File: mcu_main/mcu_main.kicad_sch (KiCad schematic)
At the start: 23 parts, among them SW1 SW_Push_Dual, SW2 SW_Push_Dual, U1 ESP32-S3-WROOM-1, U3 SGM2212-3.3, U5 SGM2212-2.8

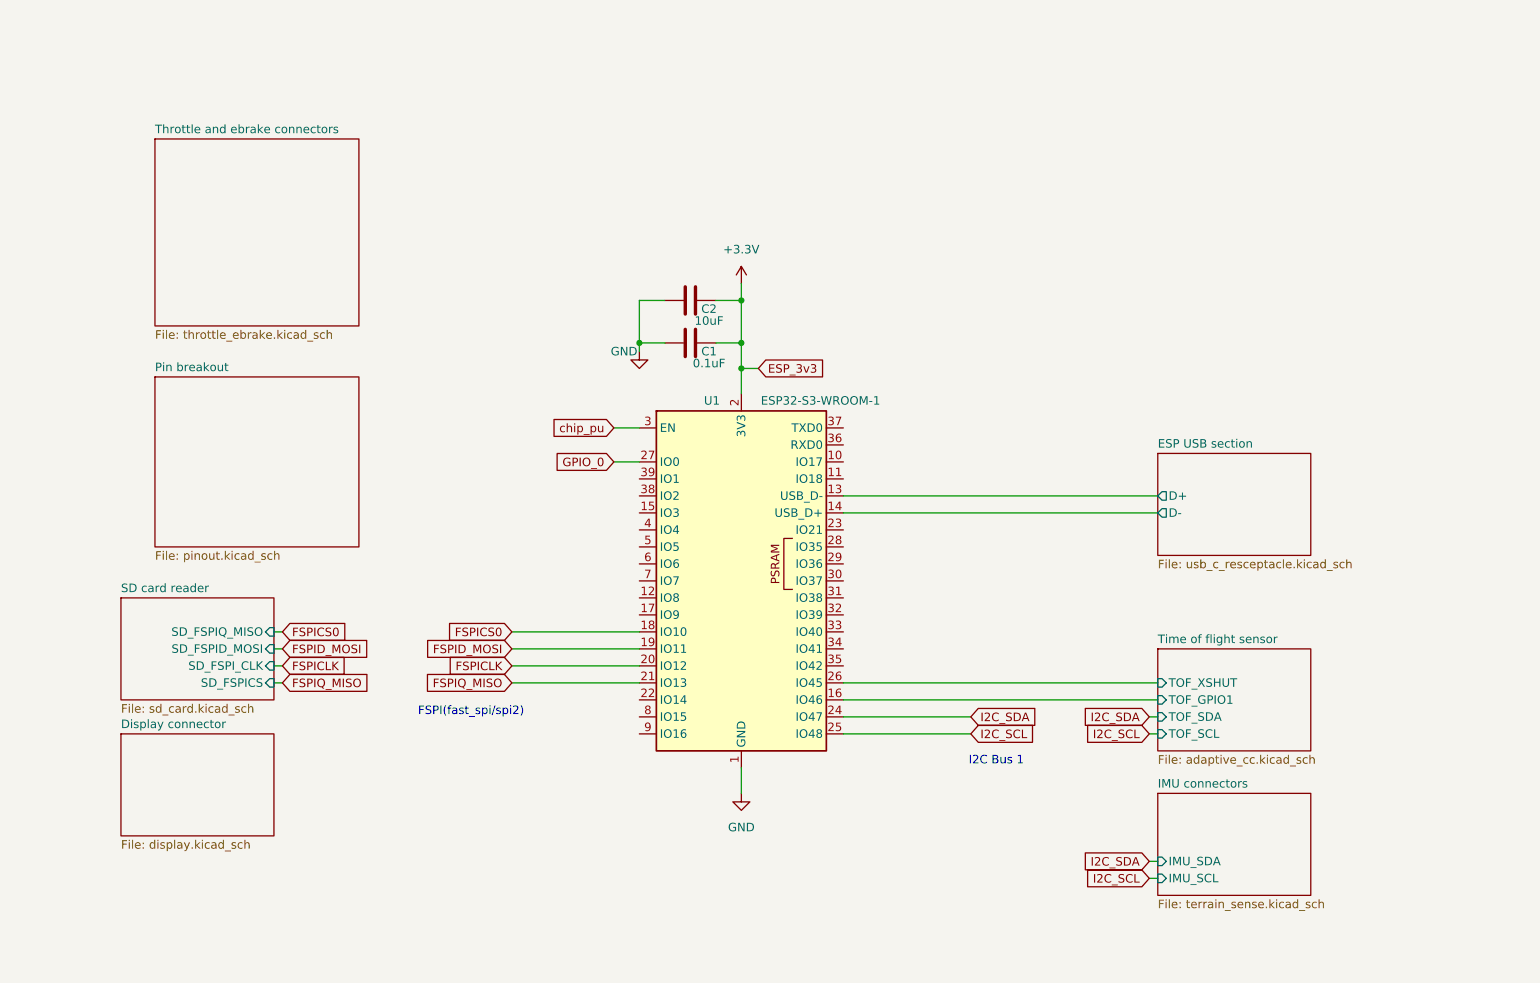
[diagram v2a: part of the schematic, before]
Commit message: added throttle and ebrake connectors
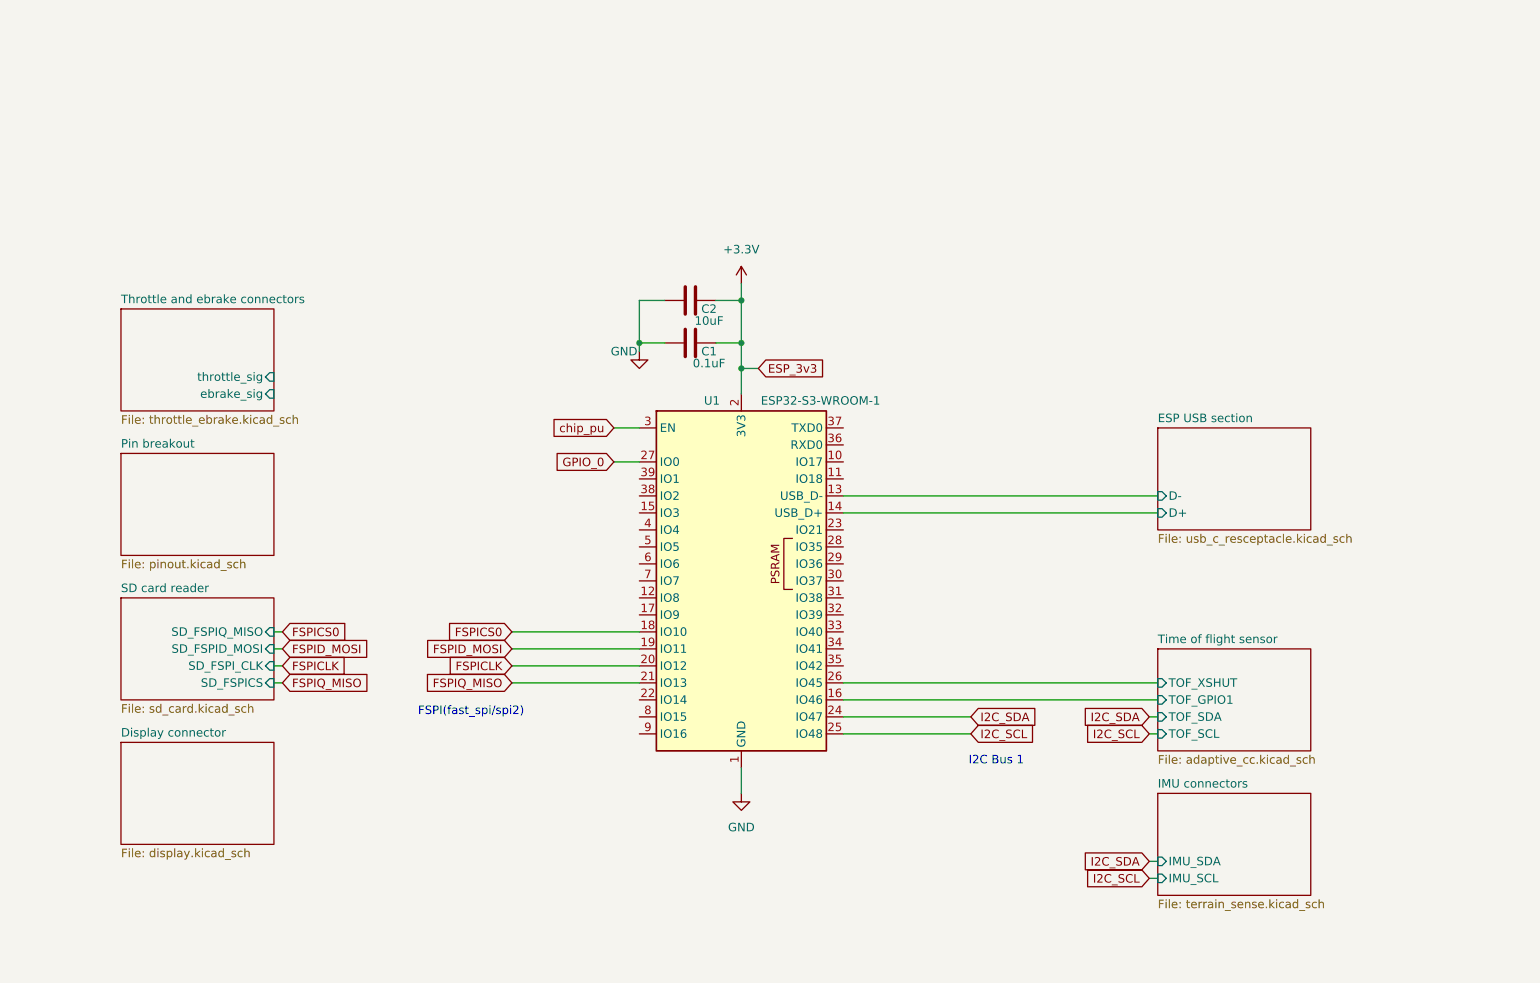
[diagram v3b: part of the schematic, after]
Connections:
- net ESP USB section/D+: now also U1.14 (USB_D+); no longer U1.13 (USB_D-)
- net ESP USB section/D-: now also U1.13 (USB_D-); no longer U1.14 (USB_D+)
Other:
- sheet Throttle and ebrake connectors ports: added ebrake_sig, throttle_sig; removed none
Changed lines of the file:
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@@
 	(wire
 		(pts
+			(xy 156.21 137.16) (xy 203.2 137.16)
+		)
+		(stroke
+			(width 0)
+			(type default)
+		)
+	)
+	(wire
+		(pts
 			(xy 196.85 246.38) (xy 199.39 246.38)
 		)
@@
 	(wire
 		(pts
-			(xy 156.21 137.16) (xy 203.2 137.16)
+			(xy 72.39 157.48) (xy 71.12 157.48)
 		)
 		(stroke
@@
 	(wire
 		(pts
-			(xy 72.39 157.48) (xy 71.12 157.48)
+			(xy 156.21 134.62) (xy 203.2 134.62)
 		)
 		(stroke
@@
 	(wire
 		(pts
-			(xy 156.21 134.62) (xy 203.2 134.62)
-		)
-		(stroke
-			(width 0)
-			(type default)
-		)
-	)
-	(wire
-		(pts
 			(xy 74.93 261.62) (xy 82.55 261.62)
 		)
@@
 		(polyline
 			(pts
-				(xy 187.006 172.7397) (xy 173.99 172.72) (xy 173.9833 164.8667) (xy 186.9993 164.8864)
+				(xy 107.9651 165.0633) (xy 91.4551 165.0633) (xy 91.4568 152.4791) (xy 107.9668 152.4791)
 			)
 			(stroke
@@
 		(polyline
 			(pts
-				(xy 60.96 248.92) (xy 60.96 281.94) (xy 105.41 281.94) (xy 105.41 248.92)
+				(xy 107.1678 240.0057) (xy 107.1678 281.9157) (xy 128.27 281.94) (xy 128.27 240.03)
 			)
 			(stroke
@@
 		(polyline
 			(pts
-				(xy 107.1678 240.0057) (xy 107.1678 281.9157) (xy 128.27 281.94) (xy 128.27 240.03)
+				(xy 214.63 233.68) (xy 214.63 281.94) (xy 295.91 281.94) (xy 295.91 233.68)
 			)
 			(stroke
@@
 		(polyline
 			(pts
-				(xy 214.63 233.68) (xy 214.63 281.94) (xy 295.91 281.94) (xy 295.91 233.68)
+				(xy 130.81 233.68) (xy 130.81 281.94) (xy 212.09 281.94) (xy 212.09 233.68)
 			)
 			(stroke
@@
 		(polyline
 			(pts
-				(xy 107.9651 165.0633) (xy 91.4551 165.0633) (xy 91.4568 152.4791) (xy 107.9668 152.4791)
+				(xy 60.96 248.92) (xy 60.96 281.94) (xy 105.41 281.94) (xy 105.41 248.92)
 			)
 			(stroke
@@
 		(polyline
 			(pts
-				(xy 15.24 248.92) (xy 15.24 281.94) (xy 58.42 281.94) (xy 58.42 248.92)
+				(xy 187.006 172.7397) (xy 173.99 172.72) (xy 173.9833 164.8667) (xy 186.9993 164.8864)
 			)
 			(stroke
@@
 		(polyline
 			(pts
-				(xy 130.81 233.68) (xy 130.81 281.94) (xy 212.09 281.94) (xy 212.09 233.68)
+				(xy 15.24 248.92) (xy 15.24 281.94) (xy 58.42 281.94) (xy 58.42 248.92)
 			)
 			(stroke
@@
 	)
 	(sheet
-		(at 48.26 170.18)
+		(at 48.26 171.45)
 		(size 22.86 15.24)
 		(exclude_from_sim no)
@@
 		)
 		(property "Sheetname" "Display connector"
-			(at 48.26 169.4684 0)
+			(at 48.26 170.7384 0)
 			(effects
 				(font
@@
 		)
 		(property "Sheetfile" "display.kicad_sch"
-			(at 48.26 186.0046 0)
+			(at 48.26 187.2746 0)
 			(effects
 				(font
@@
 	)
 	(sheet
-		(at 203.2 128.27)
+		(at 203.2 124.46)
 		(size 22.86 15.24)
 		(exclude_from_sim no)
@@
 		)
 		(property "Sheetname" "ESP USB section"
-			(at 203.2 127.5584 0)
+			(at 203.2 123.7484 0)
 			(effects
 				(font
@@
 		)
 		(property "Sheetfile" "usb_c_resceptacle.kicad_sch"
-			(at 203.2 144.0946 0)
+			(at 203.2 140.2846 0)
 			(effects
 				(font
@@
 			)
 		)
-		(pin "D+" output
-			(at 203.2 134.62 180)
+		(pin "D+" input
+			(at 203.2 137.16 180)
 			(effects
 				(font
@@
 			)
 		)
-		(pin "D-" output
-			(at 203.2 137.16 180)
+		(pin "D-" input
+			(at 203.2 134.62 180)
 			(effects
 				(font
@@
 	)
 	(sheet
-		(at 53.34 81.28)
-		(size 30.48 27.94)
+		(at 48.26 106.68)
+		(size 22.86 15.24)
 		(exclude_from_sim no)
 		(in_bom yes)
@@
 		)
 		(property "Sheetname" "Throttle and ebrake connectors"
-			(at 53.34 80.5684 0)
+			(at 48.26 105.9684 0)
 			(effects
 				(font
@@
 		)
 		(property "Sheetfile" "throttle_ebrake.kicad_sch"
-			(at 53.34 109.8046 0)
+			(at 48.26 122.5046 0)
 			(effects
 				(font
@@
 			)
 		)
+		(pin "ebrake_sig" input
+			(at 71.12 119.38 0)
+			(effects
+				(font
+					(size 1.27 1.27)
+				)
+				(justify right)
+			)
+		)
+		(pin "throttle_sig" input
+			(at 71.12 116.84 0)
+			(effects
+				(font
+					(size 1.27 1.27)
+				)
+				(justify right)
+			)
+		)
 		(instances
 			(project "mcu_main"
@@
 	)
 	(sheet
-		(at 53.34 116.84)
-		(size 30.48 25.4)
+		(at 48.26 128.27)
+		(size 22.86 15.24)
 		(exclude_from_sim no)
 		(in_bom yes)
@@
 		)
 		(property "Sheetname" "Pin breakout"
-			(at 53.34 116.1284 0)
+			(at 48.26 127.5584 0)
 			(effects
 				(font
@@
 		)
 		(property "Sheetfile" "pinout.kicad_sch"
-			(at 53.34 142.8246 0)
+			(at 48.26 144.0946 0)
 			(effects
 				(font
